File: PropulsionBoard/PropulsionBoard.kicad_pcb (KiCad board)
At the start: 2 copper layers, 68.6 x 81.3 mm, 99 parts, among them J1 Programming Header, J2 CAN_Connector, J3 Valve Connection, J4 Conn_01x03_Female, J5 Conn_01x03_Female, J6 Conn_01x03_Female, J7 Conn_01x02_Female-Connector, J8 Conn_01x02_Female-Connector, J9 Conn_01x03_Female, Q1 SI3420A-TP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

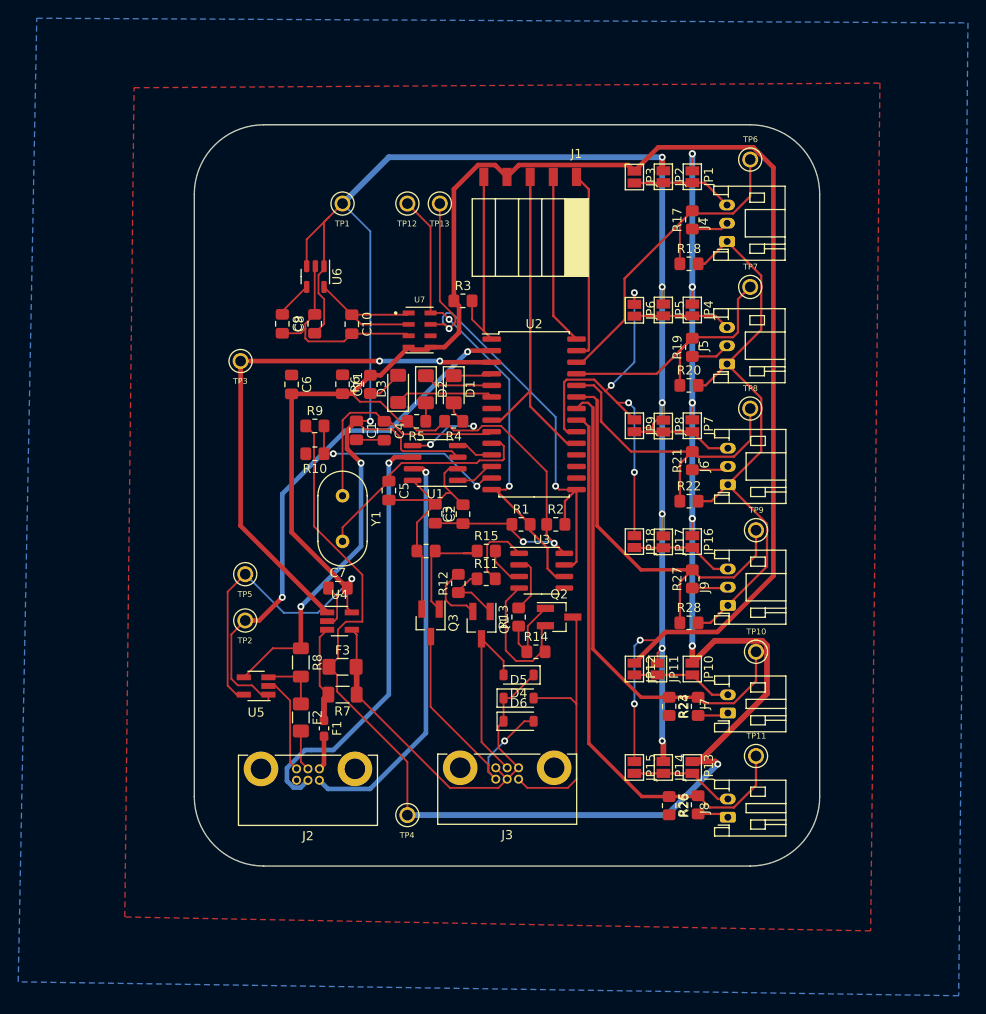
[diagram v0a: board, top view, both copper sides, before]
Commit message: updated version, layout is all routed now, and DRC errors are also resolved
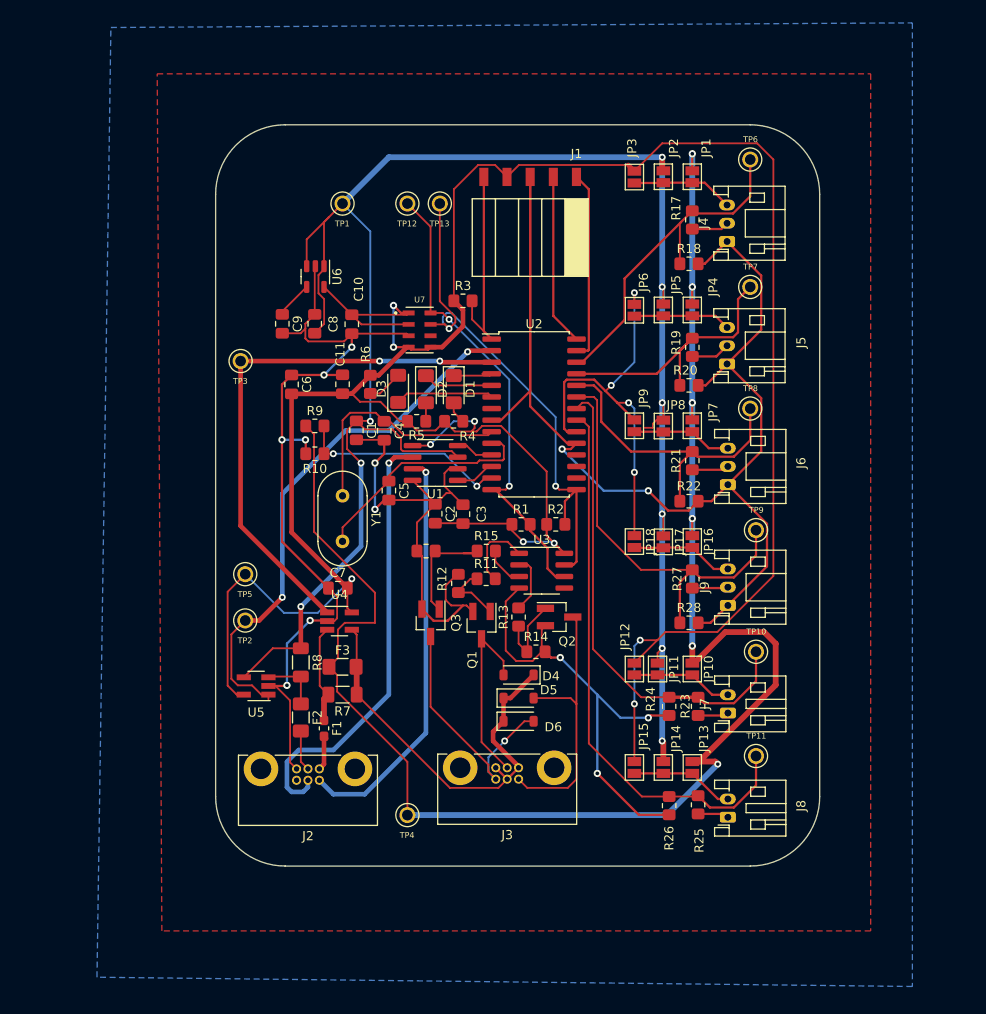
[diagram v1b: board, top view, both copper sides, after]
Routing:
- net GND: track 220.4 -> 344.7 mm, vias 0 -> 13
- net +3V3: track 335.8 -> 346.0 mm, vias 11 -> 13
- net +12V: track 180.0 -> 184.2 mm
- net CANL: track 47.1 -> 48.8 mm
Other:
- board size 68.6 x 81.3 mm -> 66.2 x 81.3 mm

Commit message: Second Revision of the Propulsion Board PCB
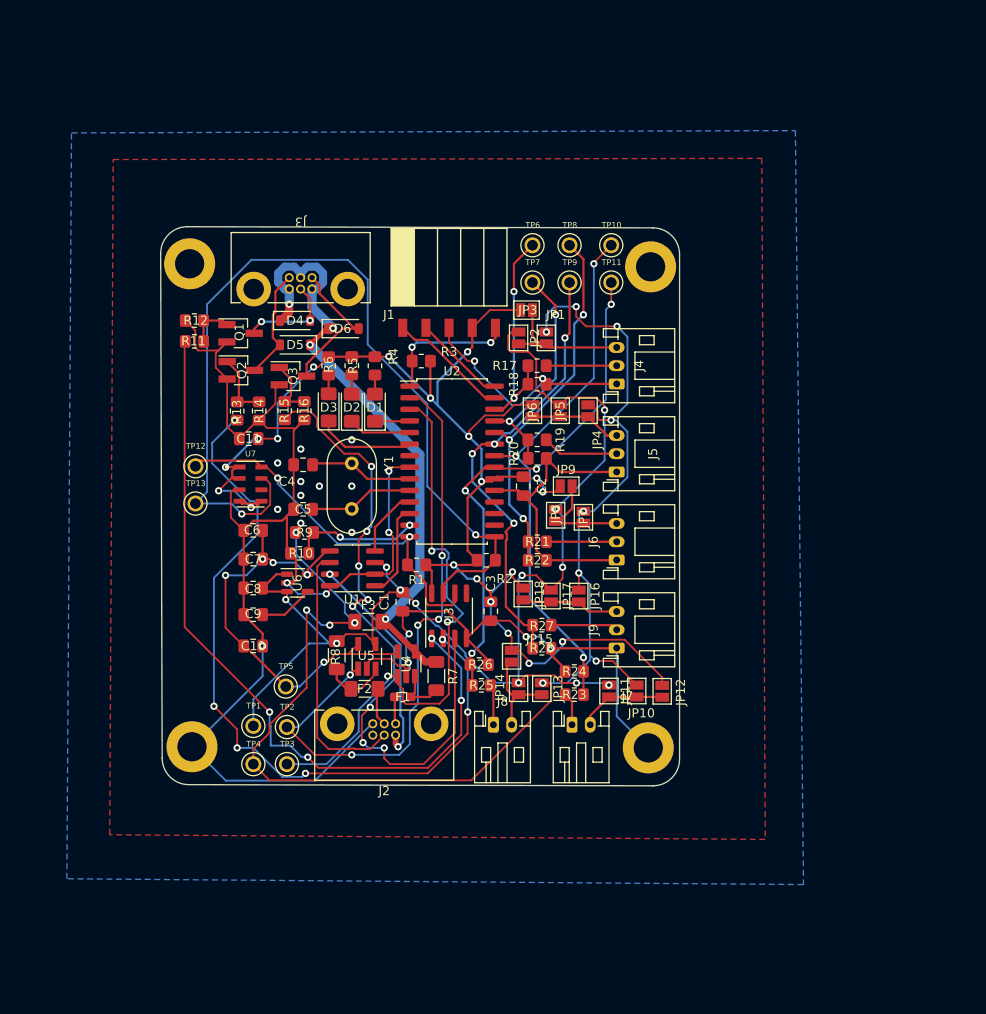
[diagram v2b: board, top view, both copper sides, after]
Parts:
- added ?: , , F.Cu at (116.3, 66.0)
- added ?: , , F.Cu at (166.6, 119.1)
- added ?: , , F.Cu at (166.9, 66.4)
- added ?: , , F.Cu at (116.6, 119.0)
- added G***: LOGO, sensor_mini:Logo_SilkScreen_5mm, B.Cu at (165.9, 97.8)
- moved TP1 58.1 mm to (123.3, 116.7), turned to 0 degrees
- moved J3 57.2 mm to (128.5, 68.8), turned to 180 degrees
- moved TP11 54.3 mm to (162.6, 68.1)
- moved TP10 47.3 mm to (162.6, 64.0)
- moved D6 47.1 mm to (133.2, 73.2)
- moved D4 45.9 mm to (127.9, 72.3), turned to 0 degrees
- moved D5 45.8 mm to (127.9, 74.9), turned to 180 degrees
- moved TP3 44.5 mm to (127.0, 120.9), turned to 0 degrees
- moved Q2 44.2 mm to (121.9, 77.7)
- moved TP13 42.4 mm to (117.0, 92.3), turned to 0 degrees
- moved Q1 41.5 mm to (121.9, 73.7), turned to 0 degrees
- moved R11 41.2 mm to (116.9, 74.5), turned to 180 degrees
- moved R12 40.8 mm to (116.9, 72.3), turned to 180 degrees
- moved R14 40.2 mm to (124.0, 82.2), turned to -90 degrees
- moved R13 38.2 mm to (121.5, 82.2), turned to -90 degrees
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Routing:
- net +3V3: track 346.0 -> 205.4 mm, vias 13 -> 25
- net +5V: track 214.7 -> 132.6 mm, vias 9 -> 12
- net GND: track 344.7 -> 262.8 mm, vias 13 -> 11
- net /MCU/VALVE_CONTROL_2: track 6.37 -> 82.7 mm, vias 0 -> 6
- net /MCU/VALVE_CONTROL_1: track 8.27 -> 83.6 mm, vias 0 -> 4
- net /MCU/VALVE_CONTROL_3: track 4.44 -> 72.5 mm, vias 0 -> 8
- net /Digital Sensor Suite/SDA: track 59.5 -> 101.4 mm
- net +12V: track 184.2 -> 149.7 mm, vias 6 -> 13
- net Actuator_Power: track 45.7 -> 68.5 mm, vias 0 -> 4
- net CANH: track 45.3 -> 23.9 mm, vias 1 -> 2
- net CANL: track 48.8 -> 28.9 mm, vias 1 -> 0
- net /Valve Control/RELAY2_-: track 30.0 -> 12.4 mm
- net /MCU/OSC1: track 26.2 -> 11.4 mm
- net /MCU/OSC2: track 25.6 -> 11.5 mm
- net /Analog Sensor/SENSOR1: track 38.1 -> 24.5 mm, vias 0 -> 2
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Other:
- board size 66.2 x 81.3 mm -> 56.9 x 61.3 mm
- board text added: "02-20-2024"
- board text added: "Krish Patel Aidan Bilon"
- board text added: "Propulsion Board"
- board text added: "Wilson Cheng"

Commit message: Third Revision of the Propulsion Board PCB
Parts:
- D1, D2, D3, F1, JP11, JP16, R4, R5, R6: moved to B.Cu
- moved G*** 1.28 mm to (167.1, 97.7)
- moved R17 0.30 mm to (154.4, 76.9)
- moved JP5 0.28 mm to (157.2, 82.0)
- moved JP6 0.13 mm to (153.8, 82.2)
- moved R15 0.13 mm to (126.9, 82.2)
- moved R14 0.13 mm to (123.8, 82.2)
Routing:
- net Actuator_Power: track 68.5 -> 76.3 mm, vias 4 -> 5
- net /MCU/VALVE_CONTROL_2: track 82.7 -> 87.0 mm
- net Net-(J7-Pin_2): track 9.75 -> 13.1 mm
- net GND: track 262.8 -> 265.4 mm, vias 11 -> 20
- net Net-(J9-Pin_3): track 10.8 -> 12.9 mm, vias 0 -> 1
- net /Analog Sensor/SENSOR4: track 49.8 -> 51.8 mm
- net CANH: track 23.9 -> 25.6 mm
- net +5V: track 132.6 -> 134.1 mm, vias 12 -> 11
- net /MCU/VALVE_CONTROL_1: track 83.6 -> 85.1 mm
- net Net-(U4-IN+): track 5.59 -> 6.75 mm, vias 0 -> 1
- net /MCU/CAN_TX: track 10.5 -> 11.5 mm
- net /MCU/VBAT: track 14.0 -> 15.0 mm
- net /Valve Control/RELAY1_-: track 10.9 -> 11.6 mm
- net +12V: track 149.7 -> 150.5 mm, vias 13 -> 12
- net /Digital Sensor Suite/SCL: track 40.7 -> 40.1 mm
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
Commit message: Forth Revision of the Propulsion Board PCB
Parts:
- moved Y1 0.87 mm to (135.0, 88.0)
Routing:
- net +5V: track 134.1 -> 135.6 mm
- net /MCU/VALVE_CONTROL_3: track 72.5 -> 73.2 mm
- net GND: vias 20 -> 24
- added copper zone on F.Cu, net GND
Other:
- board text added: "MCLR"
